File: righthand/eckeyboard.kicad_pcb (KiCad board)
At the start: 2 copper layers, 174.4 x 98.2 mm, 71 parts, among them J4 Conn_01x06_Male, J5 Conn_01x06_Male, U1 74HC4051, U2 NJM2742, U4 74LS138

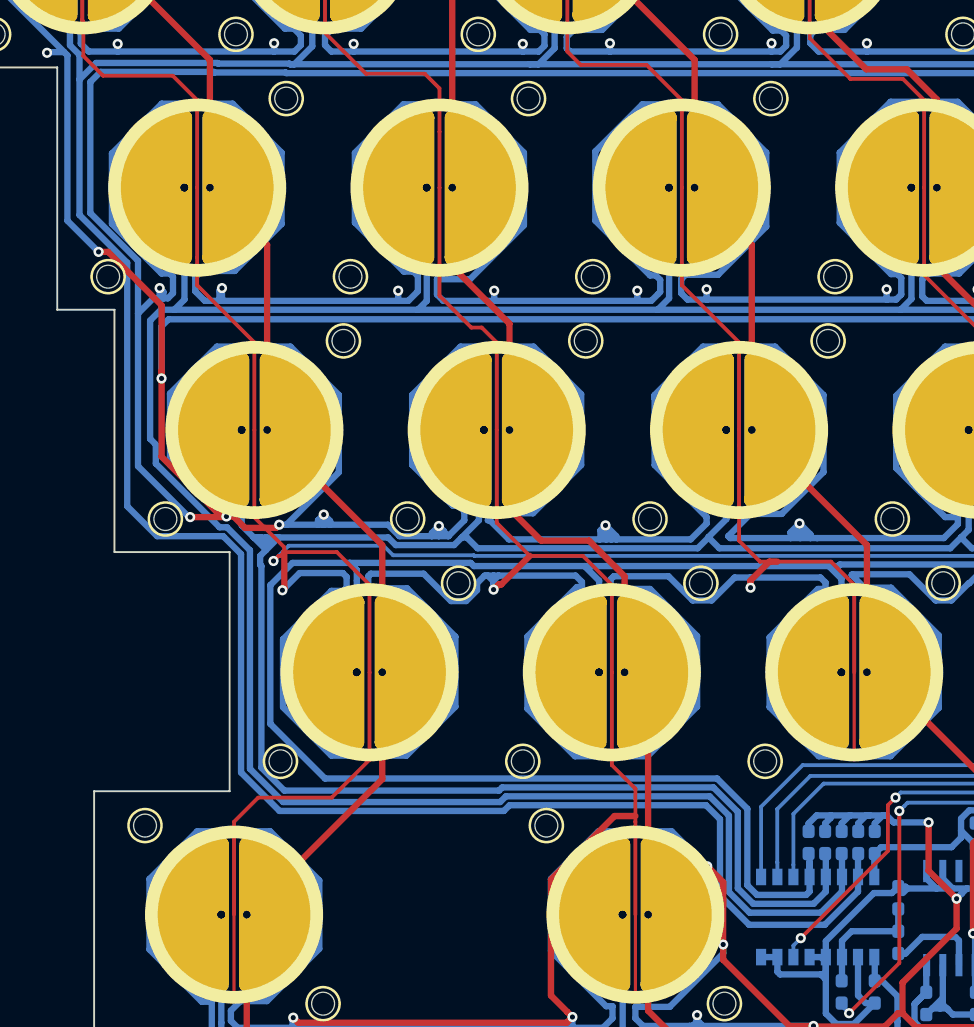
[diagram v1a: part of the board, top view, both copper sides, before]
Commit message: [fix] MUX pin ordering fix
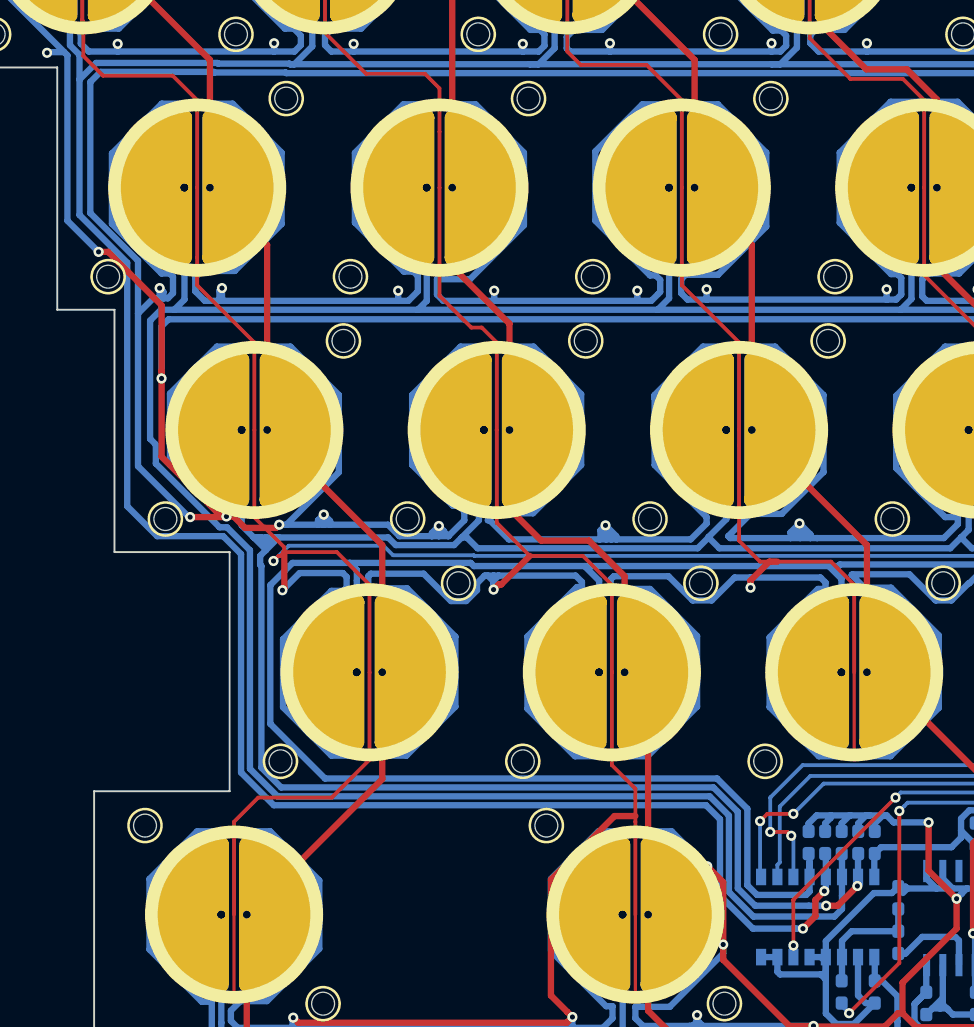
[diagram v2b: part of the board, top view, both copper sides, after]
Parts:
- TP1, TP10, TP12, TP14, TP15, TP16, TP17, TP18, TP19, TP2, TP20, TP21, TP22, TP23, TP24, TP25, TP26, TP27, TP28, TP29, TP3, TP30, TP33, TP34, TP35, TP4, TP5, TP6, TP7, TP8, TP9: value ToprePad_MntHole -> ToprePad
- TP11, TP13, TP31, TP32: value ToprePad_MntHole_B -> ToprePad
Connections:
- R1 pad 1: /ROW2 -> /ROW0
- R3 pad 1: /ROW0 -> /ROW2
- U1 pad 11: /MUX_C -> /MUX_A
- U1 pad 13: /ROW2 -> /ROW0
- U1 pad 15: /ROW0 -> /ROW2
- U1 pad 9: /MUX_A -> /MUX_C
- U2 pad 7: (no net) -> Net-(U2-Pad7)
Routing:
- net /MUX_C: track 86.1 -> 88.4 mm, vias 0 -> 2
- net /ROW2: track 311.2 -> 313.4 mm, vias 0 -> 2
- net /ROW0: track 338.0 -> 336.1 mm, vias 0 -> 2
- net /MUX_A: track 93.0 -> 94.2 mm, vias 0 -> 2
- net /ROW1: track 331.9 -> 332.5 mm
